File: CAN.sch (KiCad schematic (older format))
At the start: 19 parts

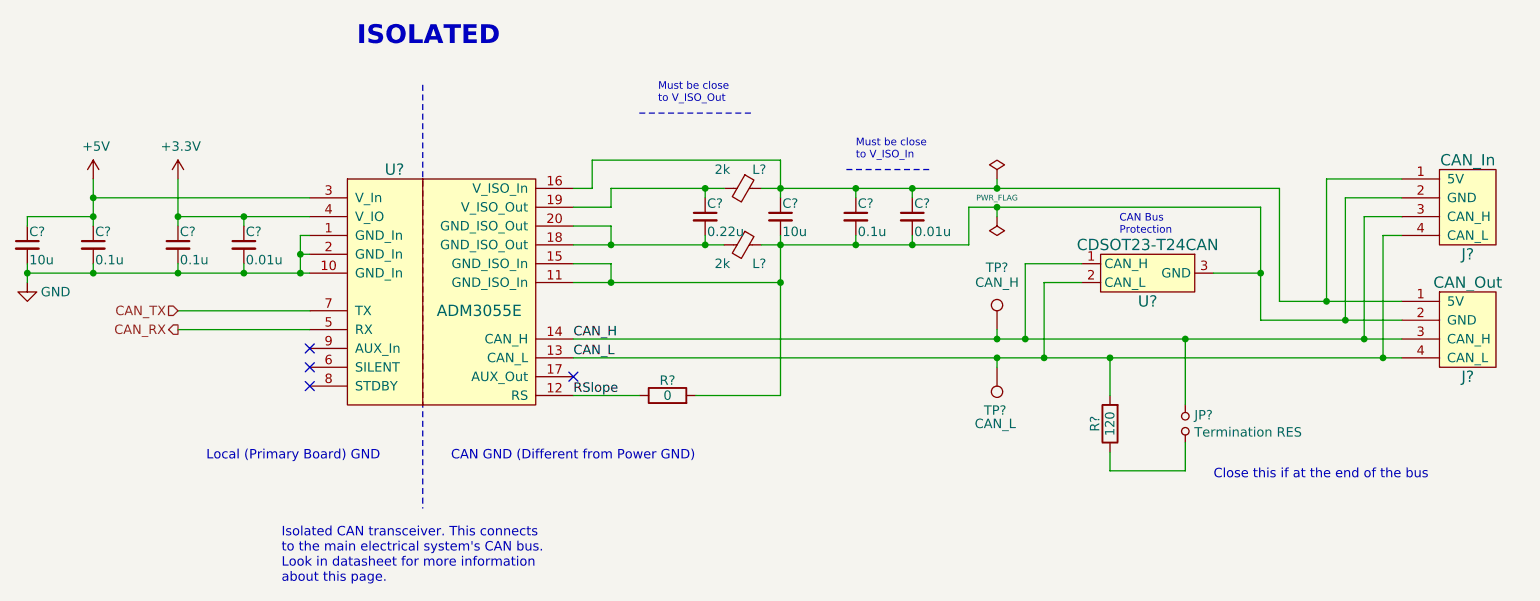
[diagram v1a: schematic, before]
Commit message: Initial layout of the Telemtry board.
The ethernet interface needs more work.
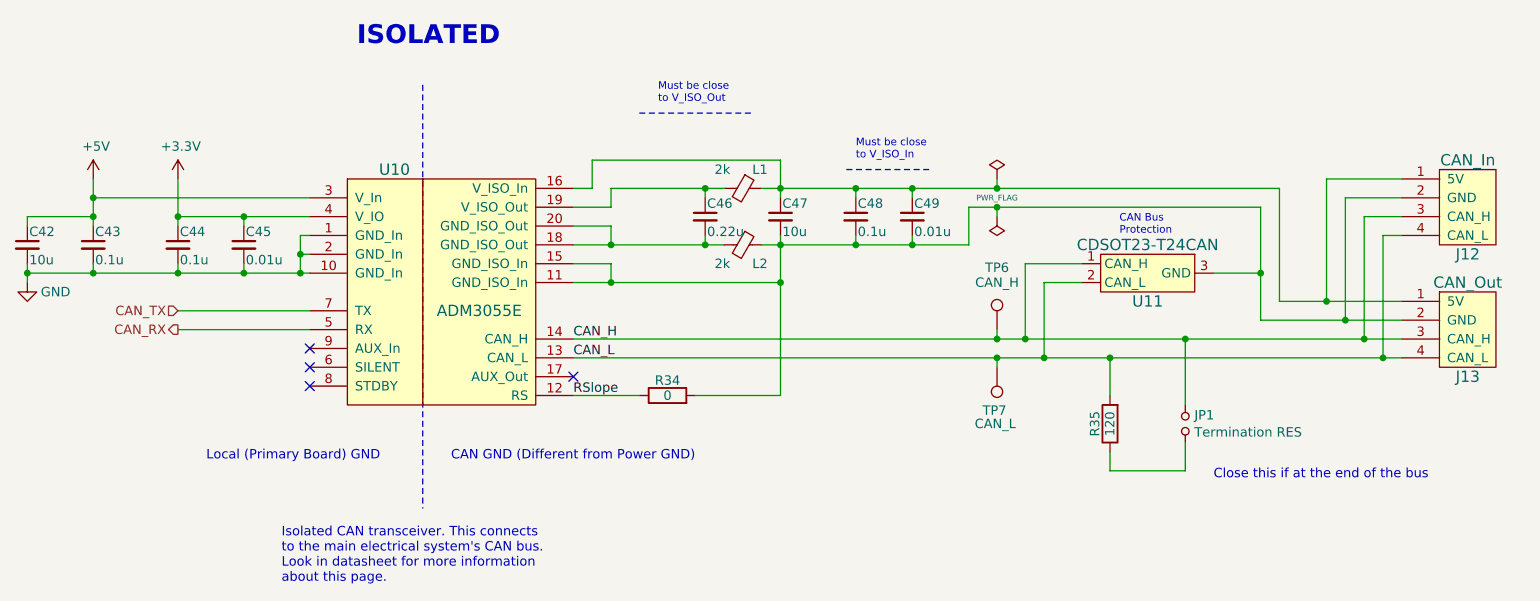
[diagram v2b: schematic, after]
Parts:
- gave numbers to parts that had none: 19
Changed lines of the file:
@@
 $EndDescr
 $Comp
-L utsvt-connectors:CANConnector J?
+L utsvt-connectors:CANConnector J13
 U 1 1 5C2B42F3
 P 9800 3800
-F 0 "J?" H 9800 3550 60  0000 C CNN
+F 0 "J13" H 9800 3550 60  0000 C CNN
 F 1 "CAN_Out" H 9800 4050 60  0000 C CNN
 F 2 "UTSVT_Connectors:Molex_MicroFit3.0_1x4xP3.00mm_PolarizingPeg_Vertical" H 9950 4100 60  0001 C CNN
@@
 $EndComp
 $Comp
-L Device:R R?
+L Device:R R35
 U 1 1 5C2B4301
 P 7900 4300
-F 0 "R?" V 7980 4300 50  0000 C CNN
+F 0 "R35" V 7980 4300 50  0000 C CNN
 F 1 "120" V 7900 4300 50  0000 C CNN
 F 2 "Resistor_SMD:R_0805_2012Metric" V 7830 4300 50  0001 C CNN
@@
 $EndComp
 $Comp
-L Device:C_Small C?
+L Device:C_Small C42
 U 1 1 5C2B4310
 P 2150 3350
-F 0 "C?" H 2160 3420 50  0000 L CNN
+F 0 "C42" H 2160 3420 50  0000 L CNN
 F 1 "10u" H 2160 3270 50  0000 L CNN
 F 2 "Capacitor_SMD:C_0805_2012Metric" H 2150 3350 50  0001 C CNN
@@
 $EndComp
 $Comp
-L Device:C_Small C?
+L Device:C_Small C43
 U 1 1 5C2B4317
 P 2500 3350
-F 0 "C?" H 2510 3420 50  0000 L CNN
+F 0 "C43" H 2510 3420 50  0000 L CNN
 F 1 "0.1u" H 2510 3270 50  0000 L CNN
 F 2 "Capacitor_SMD:C_0805_2012Metric" H 2500 3350 50  0001 C CNN
@@
 $EndComp
 $Comp
-L Device:C_Small C?
+L Device:C_Small C44
 U 1 1 5C2B431E
 P 2950 3350
-F 0 "C?" H 2960 3420 50  0000 L CNN
+F 0 "C44" H 2960 3420 50  0000 L CNN
 F 1 "0.1u" H 2960 3270 50  0000 L CNN
 F 2 "Capacitor_SMD:C_0805_2012Metric" H 2950 3350 50  0001 C CNN
@@
 $EndComp
 $Comp
-L Device:C_Small C?
+L Device:C_Small C45
 U 1 1 5C2B4325
 P 3300 3350
-F 0 "C?" H 3310 3420 50  0000 L CNN
+F 0 "C45" H 3310 3420 50  0000 L CNN
 F 1 "0.01u" H 3310 3270 50  0000 L CNN
 F 2 "Capacitor_SMD:C_0805_2012Metric" H 3300 3350 50  0001 C CNN
@@
 $EndComp
 $Comp
-L Device:C_Small C?
+L Device:C_Small C47
 U 1 1 5C2B432E
 P 6150 3200
-F 0 "C?" H 6160 3270 50  0000 L CNN
+F 0 "C47" H 6160 3270 50  0000 L CNN
 F 1 "10u" H 6160 3120 50  0000 L CNN
 F 2 "Capacitor_SMD:C_0805_2012Metric" H 6150 3200 50  0001 C CNN
@@
 $EndComp
 $Comp
-L Device:C_Small C?
+L Device:C_Small C46
 U 1 1 5C2B4335
 P 5750 3200
-F 0 "C?" H 5760 3270 50  0000 L CNN
+F 0 "C46" H 5760 3270 50  0000 L CNN
 F 1 "0.22u" H 5760 3120 50  0000 L CNN
 F 2 "Capacitor_SMD:C_0805_2012Metric" H 5750 3200 50  0001 C CNN
@@
 $EndComp
 $Comp
-L Device:Ferrite_Bead_Small L?
+L Device:Ferrite_Bead_Small L1
 U 1 1 5C2B433C
 P 5950 3050
-F 0 "L?" V 5850 3100 50  0000 L CNN
+F 0 "L1" V 5850 3100 50  0000 L CNN
 F 1 "2k" V 5850 2900 50  0000 L CNN
 F 2 "Inductor_SMD:L_0805_2012Metric" V 5880 3050 50  0001 C CNN
@@
 $EndComp
 $Comp
-L Device:Ferrite_Bead_Small L?
+L Device:Ferrite_Bead_Small L2
 U 1 1 5C2B4343
 P 5950 3350
-F 0 "L?" V 6050 3400 50  0000 L CNN
+F 0 "L2" V 6050 3400 50  0000 L CNN
 F 1 "2k" V 6050 3200 50  0000 L CNN
 F 2 "Inductor_SMD:L_0805_2012Metric" V 5880 3350 50  0001 C CNN
@@
 $EndComp
 $Comp
-L Device:C_Small C?
+L Device:C_Small C48
 U 1 1 5C2B434A
 P 6550 3200
-F 0 "C?" H 6560 3270 50  0000 L CNN
+F 0 "C48" H 6560 3270 50  0000 L CNN
 F 1 "0.1u" H 6560 3120 50  0000 L CNN
 F 2 "Capacitor_SMD:C_0805_2012Metric" H 6550 3200 50  0001 C CNN
@@
 $EndComp
 $Comp
-L Device:C_Small C?
+L Device:C_Small C49
 U 1 1 5C2B4351
 P 6850 3200
-F 0 "C?" H 6860 3270 50  0000 L CNN
+F 0 "C49" H 6860 3270 50  0000 L CNN
 F 1 "0.01u" H 6860 3120 50  0000 L CNN
 F 2 "Capacitor_SMD:C_0805_2012Metric" H 6850 3200 50  0001 C CNN
@@
 $EndComp
 $Comp
-L utsvt-chips:ADM3055E U?
+L utsvt-chips:ADM3055E U10
 U 1 1 5C2B4359
 P 4350 3600
-F 0 "U?" H 4100 4250 60  0000 C CNN
+F 0 "U10" H 4100 4250 60  0000 C CNN
 F 1 "ADM3055E" H 4550 3500 60  0000 C CNN
 F 2 "UTSVT_ICs:SOIC-20W_7.5x15.4mm_Pitch1.27mm" H 4350 3700 60  0001 C CNN
@@
 NoConn ~ 3650 4100
 $Comp
-L power:PWR_FLAG #FLG?
+L power:PWR_FLAG #FLG0105
 U 1 1 5C2B4394
 P 7300 3000
-F 0 "#FLG?" H 7300 3075 50  0001 C CNN
+F 0 "#FLG0105" H 7300 3075 50  0001 C CNN
 F 1 "PWR_FLAG" H 7300 2900 30  0000 C CNN
 F 2 "" H 7300 3000 50  0001 C CNN
@@
 $EndComp
 $Comp
-L power:PWR_FLAG #FLG?
+L power:PWR_FLAG #FLG0106
 U 1 1 5C2B439A
 P 7300 3200
-F 0 "#FLG?" H 7300 3275 50  0001 C CNN
+F 0 "#FLG0106" H 7300 3275 50  0001 C CNN
 F 1 "PWR_FLAG" H 7200 3150 50  0001 L CNN
 F 2 "" H 7300 3200 50  0001 C CNN
@@
 $EndComp
 $Comp
-L utsvt-chips:CDSOT23-T24CAN U?
+L utsvt-chips:CDSOT23-T24CAN U11
 U 1 1 5C2B43A0
 P 8100 3500
-F 0 "U?" H 8100 3350 60  0000 C CNN
+F 0 "U11" H 8100 3350 60  0000 C CNN
 F 1 "CDSOT23-T24CAN" H 8100 3650 60  0000 C CNN
 F 2 "Package_TO_SOT_SMD:SOT-23W" H 8100 3500 60  0001 C CNN
@@
 CAN Bus\nProtection
 $Comp
-L Connector:TestPoint TP?
+L Connector:TestPoint TP6
 U 1 1 5C2B43B6
 P 7300 3800
-F 0 "TP?" H 7300 4100 50  0000 C BNN
+F 0 "TP6" H 7300 4100 50  0000 C BNN
 F 1 "CAN_H" H 7300 4050 50  0000 C CNN
 F 2 "TestPoint:TestPoint_Keystone_5005-5009_Compact" H 7300 3800 50  0001 C CNN
@@
 $EndComp
 $Comp
-L Connector:TestPoint TP?
+L Connector:TestPoint TP7
 U 1 1 5C2B43BD
 P 7300 4000
-F 0 "TP?" H 7250 4200 50  0000 L BNN
+F 0 "TP7" H 7250 4200 50  0000 L BNN
 F 1 "CAN_L" H 7200 4300 50  0000 L CNN
 F 2 "TestPoint:TestPoint_Keystone_5005-5009_Compact" H 7300 4000 50  0001 C CNN
@@
 $EndComp
 $Comp
-L Device:R R?
+L Device:R R34
 U 1 1 5C2B43C4
 P 5550 4150
-F 0 "R?" V 5630 4150 50  0000 C CNN
+F 0 "R34" V 5630 4150 50  0000 C CNN
 F 1 "0" V 5550 4150 50  0000 C CNN
 F 2 "Resistor_SMD:R_0805_2012Metric" V 5480 4150 50  0001 C CNN
@@
 	5250 3050 5250 3150
 $Comp
-L power:GND #PWR?
+L power:GND #PWR0173
 U 1 1 5C28BDDE
 P 2150 3550
-F 0 "#PWR?" H 2150 3300 50  0001 C CNN
+F 0 "#PWR0173" H 2150 3300 50  0001 C CNN
 F 1 "GND" H 2300 3500 50  0000 C CNN
 F 2 "" H 2150 3550 50  0001 C CNN
@@
 	2500 3000 2500 3100
 $Comp
-L power:+3.3V #PWR?
+L power:+3.3V #PWR0174
 U 1 1 5C4ABE05
 P 2950 3000
-F 0 "#PWR?" H 2950 2850 50  0001 C CNN
+F 0 "#PWR0174" H 2950 2850 50  0001 C CNN
 F 1 "+3.3V" H 2965 3173 50  0000 C CNN
 F 2 "" H 2950 3000 50  0001 C CNN
@@
 	2950 3000 2950 3200
 $Comp
-L power:+5V #PWR?
+L power:+5V #PWR0175
 U 1 1 5C4C2AB0
 P 2500 3000
-F 0 "#PWR?" H 2500 2850 50  0001 C CNN
+F 0 "#PWR0175" H 2500 2850 50  0001 C CNN
 F 1 "+5V" H 2515 3173 50  0000 C CNN
 F 2 "" H 2500 3000 50  0001 C CNN
@@
 Isolated CAN transceiver. This connects\nto the main electrical system's CAN bus.\nLook in datasheet for more information\nabout this page.
 $Comp
-L utsvt-connectors:CANConnector J?
+L utsvt-connectors:CANConnector J12
 U 1 1 5F696B9A
 P 9800 3150
-F 0 "J?" H 9800 2900 60  0000 C CNN
+F 0 "J12" H 9800 2900 60  0000 C CNN
 F 1 "CAN_In" H 9800 3400 60  0000 C CNN
 F 2 "UTSVT_Connectors:Molex_MicroFit3.0_1x4xP3.00mm_PolarizingPeg_Vertical" H 9950 3450 60  0001 C CNN
@@
 $EndComp
 $Comp
-L Device:Jumper_NO_Small JP?
+L Device:Jumper_NO_Small JP1
 U 1 1 5F69FB6B
 P 8300 4300
-F 0 "JP?" V 8254 4348 50  0000 L CNN
+F 0 "JP1" V 8254 4348 50  0000 L CNN
 F 1 "Termination RES" V 8345 4348 50  0000 L CNN
 F 2 "Connector_PinHeader_2.54mm:PinHeader_1x02_P2.54mm_Vertical" H 8300 4300 50  0001 C CNN
